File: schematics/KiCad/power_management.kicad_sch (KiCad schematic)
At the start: 39 parts, among them J3 USB_C, Q1 DMG6601LVT-7, Q2 DMG6601LVT-7, SW4 TL1105SF160R, U4 AP2112K-3.3, U5 MP2615AGQ-Z

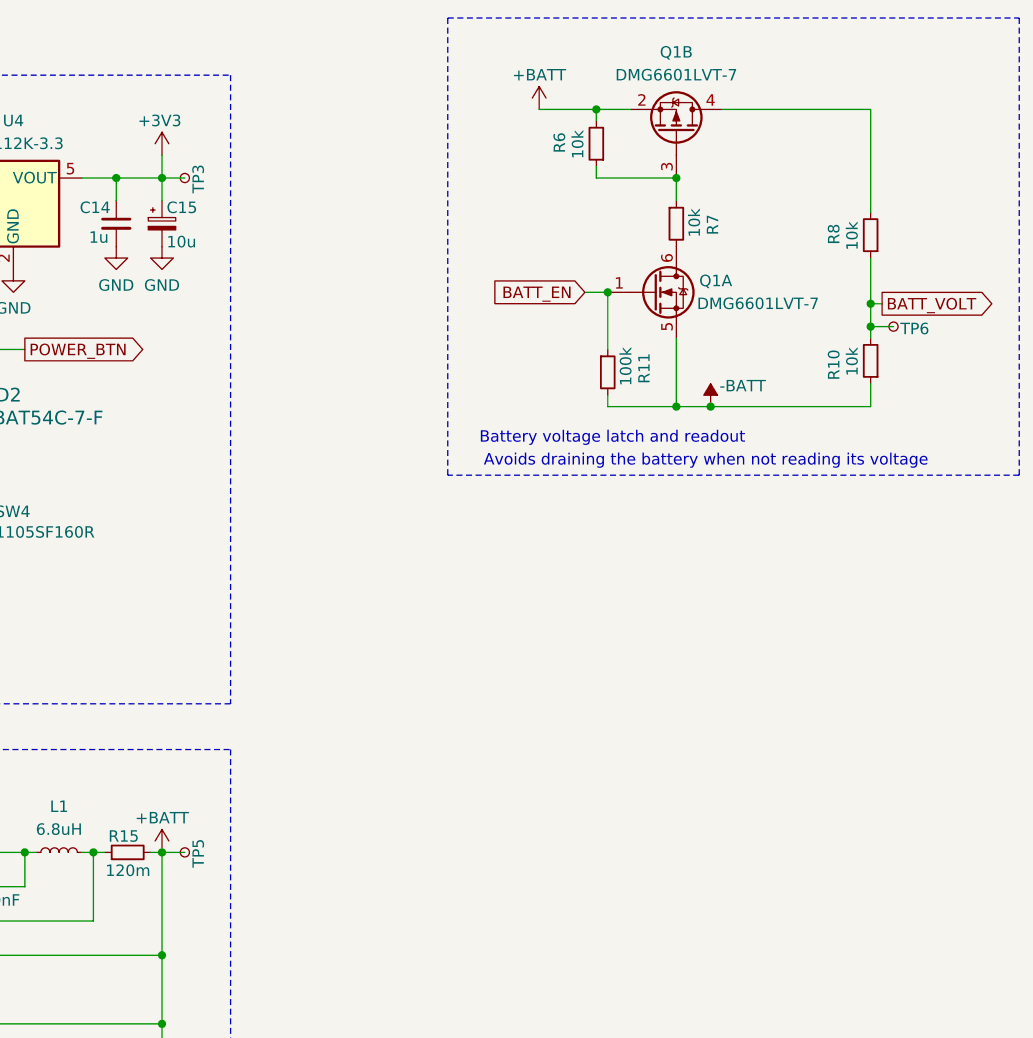
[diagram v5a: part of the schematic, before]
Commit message: add battery test points
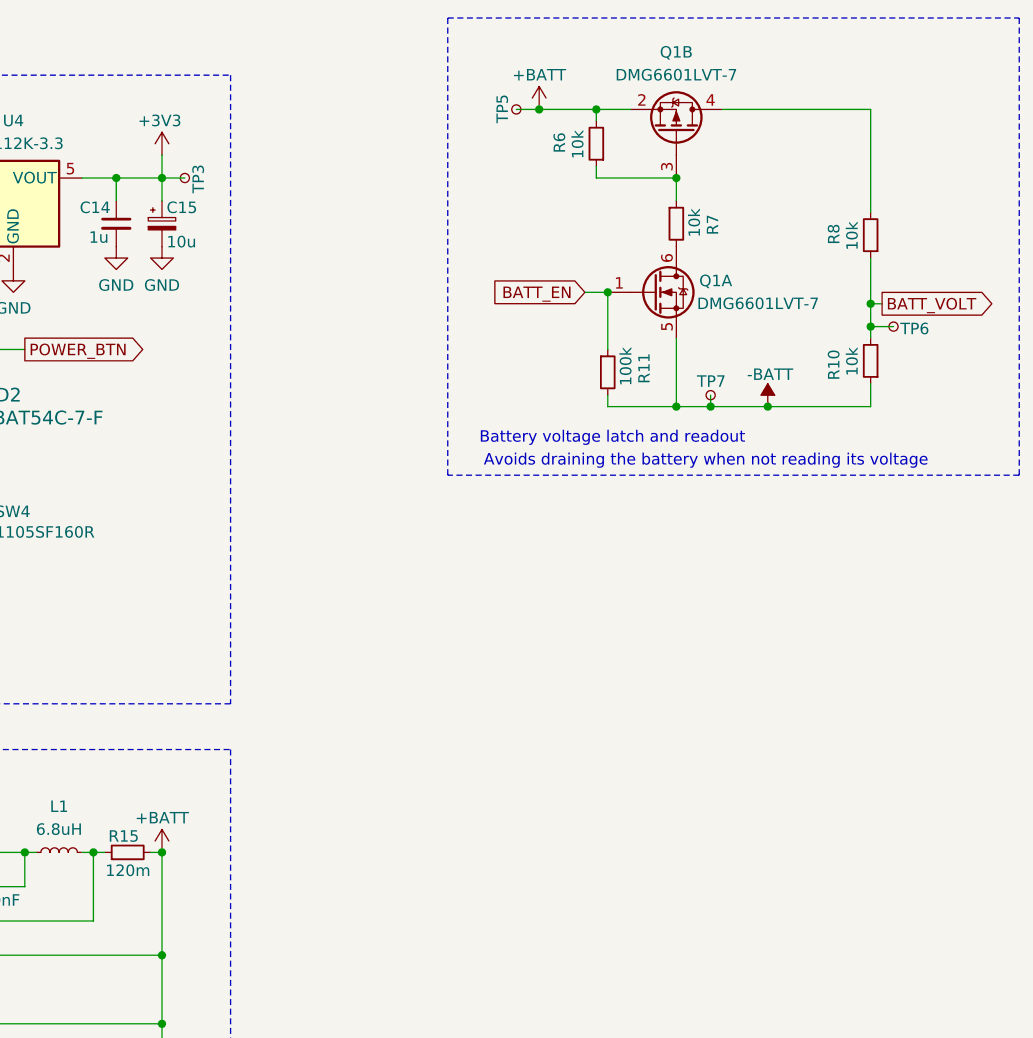
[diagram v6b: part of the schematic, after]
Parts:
- added TP7: GND, TestPoint:TestPoint_Pad_1.0x1.0mm, symbol Connector:TestPoint_Small
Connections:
- net -BATT: now also TP7.1
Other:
- moved on the sheet: TP5
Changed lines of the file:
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@@
 	)
 	(junction
+		(at 246.38 66.04)
+		(diameter 0)
+		(color 0 0 0 0)
+	)
+	(junction
 		(at 171.45 115.57)
 		(diameter 0)
@@
 	)
 	(junction
+		(at 240.03 66.04)
+		(diameter 0)
+		(color 0 0 0 0)
+	)
+	(junction
 		(at 163.83 115.57)
 		(diameter 0)
@@
 	)
 	(junction
-		(at 240.03 66.04)
-		(diameter 0)
-		(color 0 0 0 0)
-	)
-	(junction
 		(at 100.33 115.57)
 		(diameter 0)
@@
 	)
 	(junction
+		(at 220.98 33.02)
+		(diameter 0)
+		(color 0 0 0 0)
+	)
+	(junction
 		(at 118.11 59.69)
 		(diameter 0)
@@
 	(wire
 		(pts
-			(xy 240.03 66.04) (xy 257.81 66.04)
-		)
-		(stroke
-			(width 0)
-			(type default)
-		)
-	)
-	(wire
-		(pts
 			(xy 130.81 78.74) (xy 130.81 85.09)
 		)
@@
 	(wire
 		(pts
-			(xy 179.07 115.57) (xy 181.61 115.57)
-		)
-		(stroke
-			(width 0)
-			(type default)
-		)
-	)
-	(wire
-		(pts
 			(xy 138.43 73.66) (xy 140.97 73.66)
 		)
@@
 	(wire
 		(pts
+			(xy 246.38 66.04) (xy 257.81 66.04)
+		)
+		(stroke
+			(width 0)
+			(type default)
+		)
+	)
+	(wire
+		(pts
 			(xy 137.16 146.05) (xy 140.97 146.05)
 		)
@@
 	(wire
 		(pts
+			(xy 240.03 66.04) (xy 246.38 66.04)
+		)
+		(stroke
+			(width 0)
+			(type default)
+		)
+	)
+	(wire
+		(pts
 			(xy 151.13 40.64) (xy 154.94 40.64)
 		)
@@
 	(wire
 		(pts
+			(xy 218.44 33.02) (xy 220.98 33.02)
+		)
+		(stroke
+			(width 0)
+			(type default)
+		)
+	)
+	(wire
+		(pts
 			(xy 115.57 127) (xy 116.84 127)
 		)
@@
 	(wire
 		(pts
+			(xy 240.03 64.77) (xy 240.03 66.04)
+		)
+		(stroke
+			(width 0)
+			(type default)
+		)
+	)
+	(wire
+		(pts
 			(xy 154.94 40.64) (xy 154.94 43.18)
 		)
@@
 	(symbol
 		(lib_id "Connector:TestPoint_Small")
-		(at 181.61 115.57 270)
+		(at 218.44 33.02 90)
 		(unit 1)
 		(exclude_from_sim no)
@@
 		(dnp no)
 		(property "Reference" "TP5"
-			(at 183.134 114.046 0)
+			(at 216.916 34.544 0)
 			(effects
 				(font
@@
 		)
 		(property "Value" "GND"
-			(at 180.3401 116.84 0)
+			(at 219.7099 31.75 0)
 			(effects
 				(font
@@
 		)
 		(property "Footprint" "TestPoint:TestPoint_Pad_1.0x1.0mm"
-			(at 181.61 120.65 0)
+			(at 218.44 27.94 0)
 			(effects
 				(font
@@
 		)
 		(property "Datasheet" "~"
-			(at 181.61 120.65 0)
+			(at 218.44 27.94 0)
 			(effects
 				(font
@@
 		)
 		(property "Description" "test point"
-			(at 181.61 115.57 0)
+			(at 218.44 33.02 0)
 			(effects
 				(font
@@
 	(symbol
 		(lib_id "power:-BATT")
-		(at 240.03 66.04 0)
+		(at 246.38 66.04 0)
 		(unit 1)
 		(exclude_from_sim no)
@@
 		(dnp no)
 		(property "Reference" "#PWR032"
-			(at 240.03 69.85 0)
+			(at 246.38 69.85 0)
 			(effects
 				(font
@@
 		)
 		(property "Value" "-BATT"
-			(at 243.586 63.754 0)
+			(at 246.634 62.484 0)
 			(effects
 				(font
@@
 		)
 		(property "Footprint" ""
-			(at 240.03 66.04 0)
+			(at 246.38 66.04 0)
 			(effects
 				(font
@@
 		)
 		(property "Datasheet" ""
-			(at 240.03 66.04 0)
+			(at 246.38 66.04 0)
 			(effects
 				(font
@@
 		)
 		(property "Description" "Power symbol creates a global label with name \"-BATT\""
-			(at 240.03 66.04 0)
+			(at 246.38 66.04 0)
 			(effects
 				(font
@@
 					(unit 1)
 				)
+			)
+		)
+	)
+	(symbol
+		(lib_id "Connector:TestPoint_Small")
+		(at 240.03 64.77 0)
+		(unit 1)
+		(exclude_from_sim no)
+		(in_bom yes)
+		(on_board yes)
+		(dnp no)
+		(property "Reference" "TP7"
+			(at 238.506 63.246 0)
+			(effects
+				(font
+					(size 1.27 1.27)
+				)
+				(justify left)
+			)
+		)
+		(property "Value" "GND"
+			(at 241.3 66.0399 0)
+			(effects
+				(font
+					(size 1.27 1.27)
+				)
+				(justify left)
+				(hide yes)
+			)
+		)
+		(property "Footprint" "TestPoint:TestPoint_Pad_1.0x1.0mm"
+			(at 245.11 64.77 0)
+			(effects
+				(font
+					(size 1.27 1.27)
+				)
+				(hide yes)
+			)
+		)
+		(property "Datasheet" "~"
+			(at 245.11 64.77 0)
+			(effects
+				(font
+					(size 1.27 1.27)
+				)
+				(hide yes)
+			)
+		)
+		(property "Description" "test point"
+			(at 240.03 64.77 0)
+			(effects
+				(font
+					(size 1.27 1.27)
+				)
+				(hide yes)
+			)
+		)
+		(pin "1"
+		)
+		(instances
+			(project "leany"
+				(path "/e47b2519-93ca-4a48-9414-ecc253dd35f5/702fc064-eab2-4b82-8f62-a654ccd28f72"
+					(reference "TP7")
+					(unit 1)
+				)

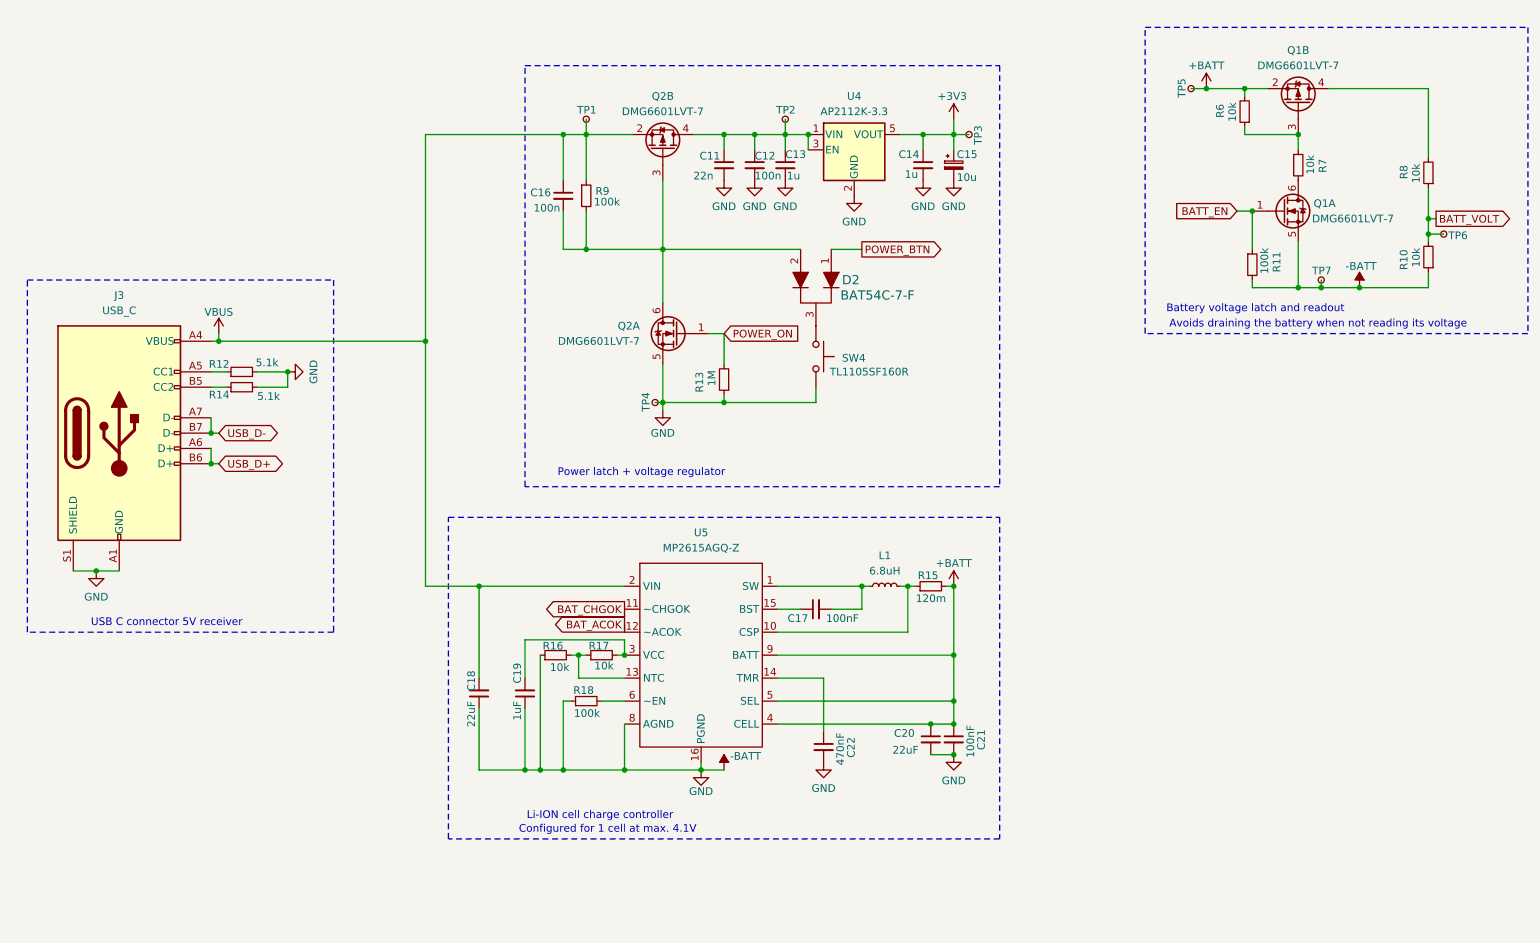
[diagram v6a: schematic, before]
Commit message: reorganise power management
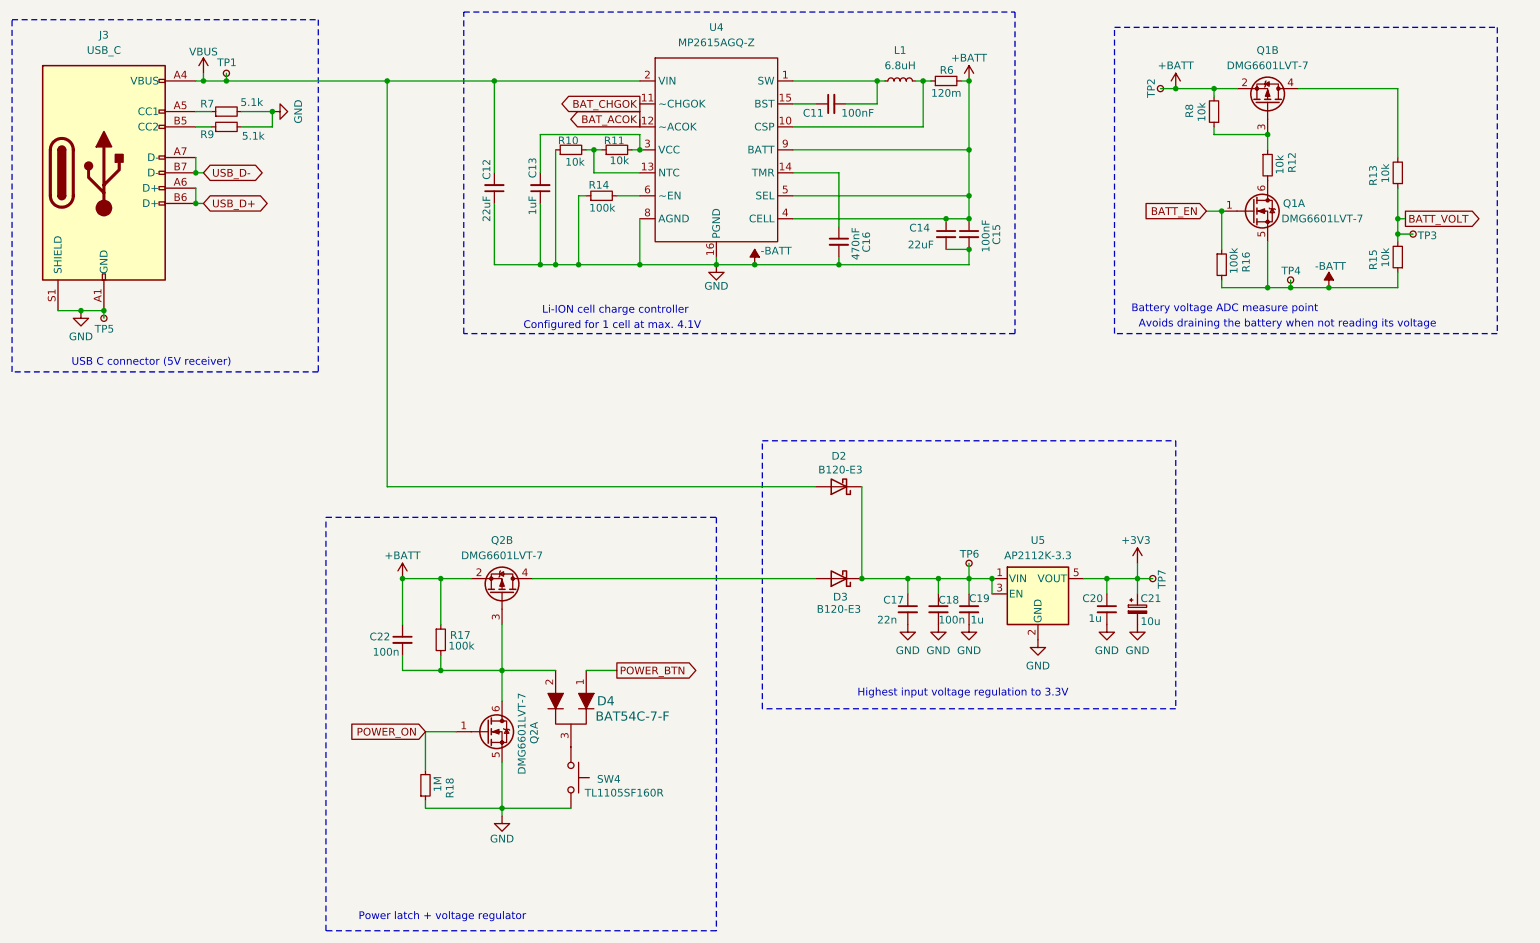
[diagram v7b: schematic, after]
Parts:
- removed C11: 22n, Capacitor_SMD:C_0201_0603Metric, symbol Device:C_Small
- removed C12: 100n, Capacitor_SMD:C_0201_0603Metric, symbol Device:C_Small
- removed C13, C14: 1u, Capacitor_SMD:C_0201_0603Metric, symbol Device:C_Small
- removed C15: 10u, symbol Device:C_Polarized_Small
- removed TP2: Vin, TestPoint:TestPoint_Pad_1.0x1.0mm, symbol Connector:TestPoint_Small
- removed TP3: 3.3V, TestPoint:TestPoint_Pad_1.0x1.0mm, symbol Connector:TestPoint_Small
- removed U4: AP2112K-3.3, Package_TO_SOT_SMD:SOT-23-5, symbol Regulator_Linear:AP2112K-3.3
- added C17: 22n, Capacitor_SMD:C_0201_0603Metric, symbol Device:C_Small
- added C18: 100n, Capacitor_SMD:C_0201_0603Metric, symbol Device:C_Small
- added C19, C20: 1u, Capacitor_SMD:C_0201_0603Metric, symbol Device:C_Small
- added C21: 10u, symbol Device:C_Polarized_Small
- added D2, D3: B120-E3, Diode_SMD:D_SMA, symbol Diode:B120-E3
- added TP6: Vin, TestPoint:TestPoint_Pad_1.0x1.0mm, symbol Connector:TestPoint_Small
- added TP7: 3.3V, TestPoint:TestPoint_Pad_1.0x1.0mm, symbol Connector:TestPoint_Small
- added U5: AP2112K-3.3, Package_TO_SOT_SMD:SOT-23-5, symbol Regulator_Linear:AP2112K-3.3
- TP1: value 5V -> GND
- renumbered C17 to C11, C18 to C12, C19 to C13, C20 to C14, C21 to C15, C22 to C16, C16 to C22, D2 to D4, R16 to R10, R17 to R11, R7 to R12, R8 to R13, R18 to R14, R10 to R15, R11 to R16, R9 to R17, R13 to R18, R15 to R6, R12 to R7, R6 to R8, R14 to R9, TP5 to TP2, TP6 to TP3, TP7 to TP4, TP4 to TP5, U5 to U4
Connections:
- net +3V3: now also C20.1, C21.1, TP7.1, U5.5 (VOUT)
- net +BATT: now also C22.1, Q2.2 (S), R17.1
- net -BATT: now also C17.2, C18.2, C19.2, C20.2, C21.2, U5.2 (GND)
- net VBUS: now also D2.2 (A); no longer C22.1, Q2.2 (S), R17.1
- net at Q2.4 (D): now also D3.2 (A)
- new net: C17.1, C18.1, C19.1, D2.1 (K), D3.1 (K), TP6.1, U5.1 (VIN), U5.3 (EN)
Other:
- note added: "Battery voltage ADC measure point"
- note added: "Highest input voltage regulation to 3.3V"
- note added: "USB C connector (5V receiver)"
- note removed: "Battery voltage latch and readout"
- note removed: "USB C connector 5V receiver"
- moved on the sheet: C11, C12, C13, C14, C15, C16, C22, D4, J3, L1, Q1A, Q1B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
